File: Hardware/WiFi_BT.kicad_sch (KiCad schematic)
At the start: 12 parts, among them J5 Conn_01x12, P1 ESP_DATA, SW5 ESP_BOOT, SW6 ESP_RST, U7 ESP32-S3-WROOM-1

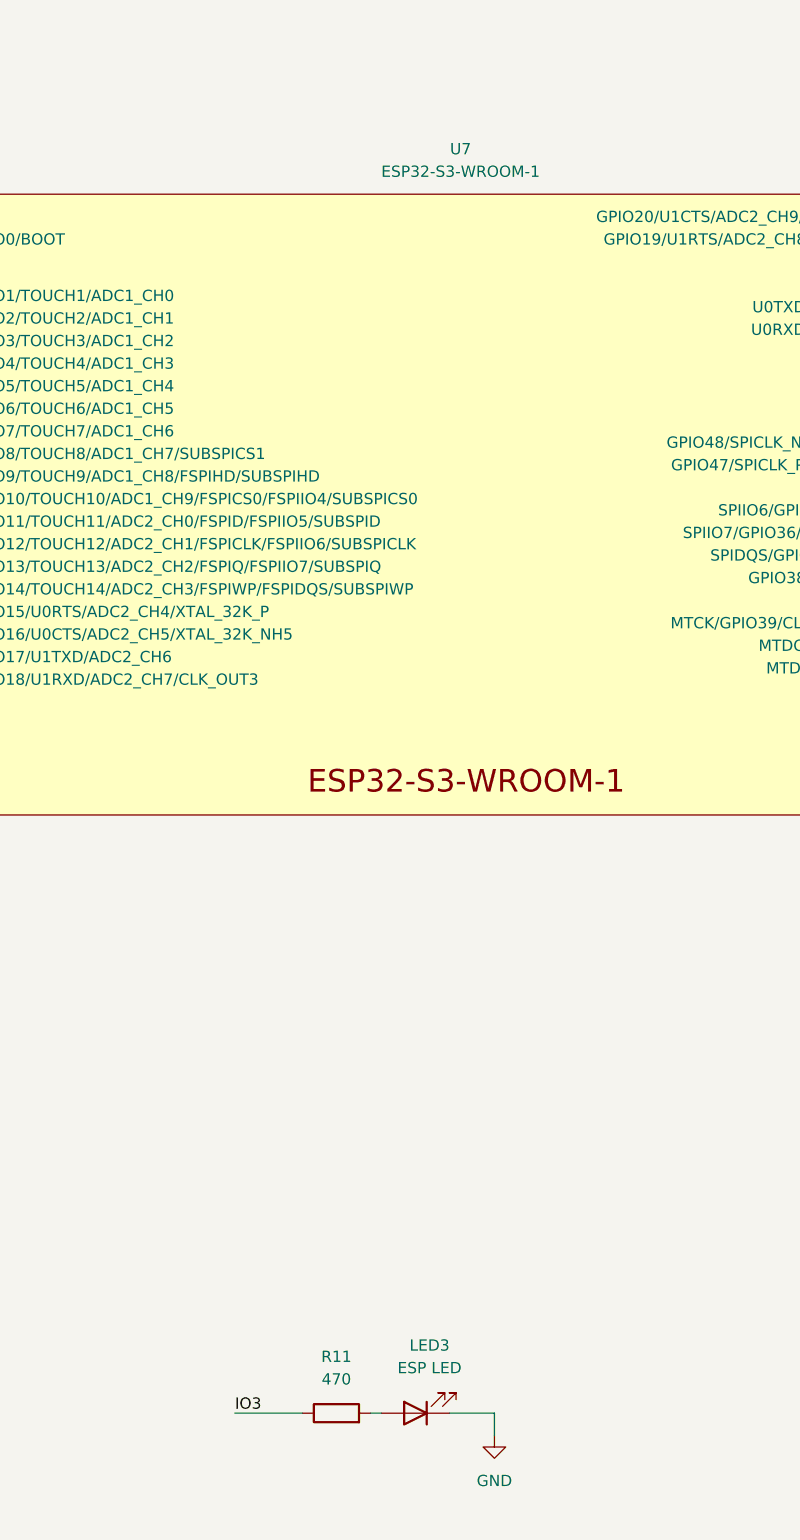
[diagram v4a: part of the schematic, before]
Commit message: TODO list completed - need to search for components
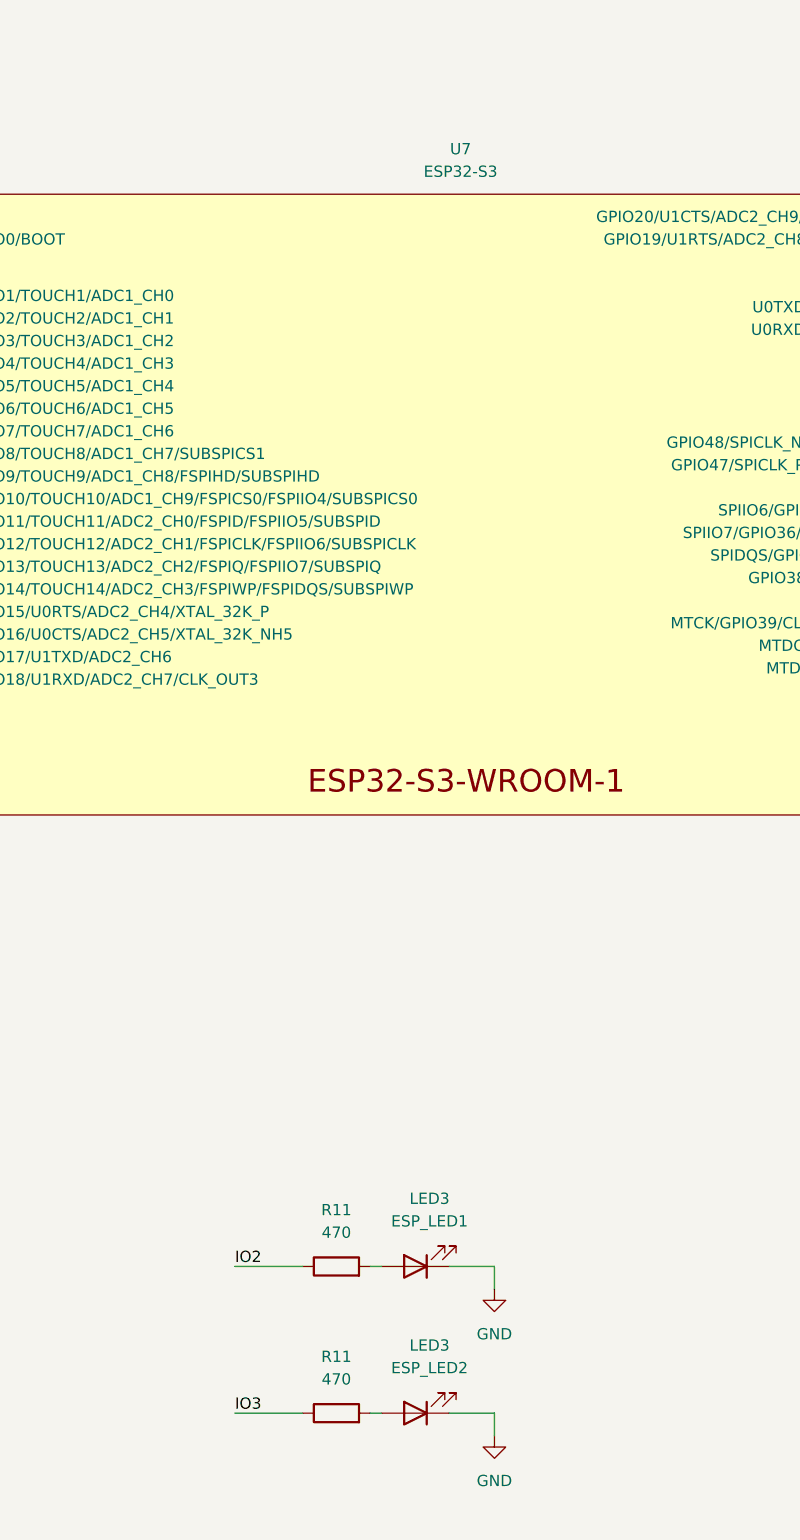
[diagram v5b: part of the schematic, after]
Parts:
- added LED3: ESP_LED1, LED_SMD:LED_0603_1608Metric, symbol Device:LED
- added R11: 470, Resistor_SMD:R_0402_1005Metric, symbol Device:R
- J5: footprint Connector_PinSocket_1.27mm:PinSocket_2x17_P1.27mm_Vertical -> Connector_PinSocket_1.27mm:PinSocket_2x16_P1.27mm_Vertical
- LED3: value ESP LED -> ESP_LED2
- U7: value ESP32-S3-WROOM-1 -> ESP32-S3
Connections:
- net GND: now also LED3.1 (K)
- net IO2: now also R11.1
- new net: LED3.2 (A), R11.2
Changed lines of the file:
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@@
   (junction (at 68.58 46.99) (diameter 0) (color 0 0 0 0)
   )
+  (wire (pts (xy 111.125 162.56) (xy 118.745 162.56))
+    (stroke (width 0) (type default))
+  )
   (wire (pts (xy 69.85 93.98) (xy 77.47 93.98))
     (stroke (width 0) (type default))
@@
     (stroke (width 0) (type default))
   )
+  (wire (pts (xy 140.335 162.56) (xy 140.335 165.1))
+    (stroke (width 0) (type default))
+  )
   (wire (pts (xy 195.58 54.61) (xy 208.28 54.61))
     (stroke (width 0) (type default))
@@
     (stroke (width 0) (type default))
   )
+  (wire (pts (xy 126.365 162.56) (xy 127.635 162.56))
+    (stroke (width 0) (type default))
+  )
   (wire (pts (xy 195.58 57.15) (xy 208.28 57.15))
     (stroke (width 0) (type default))
@@
   )
   (wire (pts (xy 195.58 92.71) (xy 203.2 92.71))
+    (stroke (width 0) (type default))
+  )
+  (wire (pts (xy 135.255 162.56) (xy 140.335 162.56))
     (stroke (width 0) (type default))
   )
@@
     (effects (font (size 1.27 1.27)) (justify right bottom))
   )
+  (label "IO2" (at 111.125 162.56 0) (fields_autoplaced)
+    (effects (font (size 1.27 1.27)) (justify left bottom))
+  )
   (label "IO40" (at 267.97 44.45 180) (fields_autoplaced)
     (effects (font (size 1.27 1.27)) (justify right bottom))
@@
       (effects (font (size 1.27 1.27)))
     )
-    (property "Value" "ESP LED" (at 133.0325 173.99 0)
+    (property "Value" "ESP_LED2" (at 133.0325 173.99 0)
       (effects (font (size 1.27 1.27)))
     )
@@
     )
   )
+  (symbol (lib_id "Device:R") (at 122.555 162.56 90) (unit 1)
+    (in_bom yes) (on_board yes) (dnp no) (fields_autoplaced)
+    (property "Reference" "R11" (at 122.555 156.21 90)
+      (effects (font (size 1.27 1.27)))
+    )
+    (property "Value" "470" (at 122.555 158.75 90)
+      (effects (font (size 1.27 1.27)))
+    )
+    (property "Footprint" "Resistor_SMD:R_0402_1005Metric" (at 122.555 164.338 90)
+      (effects (font (size 1.27 1.27)) hide)
+    )
+    (property "Datasheet" "~" (at 122.555 162.56 0)
+      (effects (font (size 1.27 1.27)) hide)
+    )
+    (pin "1")
+    (pin "2")
+    (instances
+      (project "Badge"
+        (path "/11e70834-763a-4962-b37c-877b60a06e6a"
+          (reference "R11") (unit 1)
+        )
+        (path "/11e70834-763a-4962-b37c-877b60a06e6a/439e12f3-d6d7-4417-89eb-793f278686d2"
+          (reference "R27") (unit 1)
+        )
+      )
+    )
+  )
   (symbol (lib_id "ESP32:ESP32-S3-WROOM-1") (at 137.16 76.2 0) (unit 1)
     (in_bom yes) (on_board yes) (dnp no) (fields_autoplaced)
@@
       (effects (font (size 1.27 1.27)))
     )
-    (property "Value" "ESP32-S3-WROOM-1" (at 136.525 39.37 0)
+    (property "Value" "ESP32-S3" (at 136.525 39.37 0)
       (effects (font (size 1.27 1.27)))
     )
@@
       (effects (font (size 1.27 1.27)))
     )
-    (property "Footprint" "Connector_PinSocket_1.27mm:PinSocket_2x17_P1.27mm_Vertical" (at 255.27 54.61 0)
+    (property "Footprint" "Connector_PinSocket_1.27mm:PinSocket_2x16_P1.27mm_Vertical" (at 255.27 54.61 0)
       (effects (font (size 1.27 1.27)) hide)
     )
@@
     )
   )
+  (symbol (lib_id "Device:LED") (at 131.445 162.56 180) (unit 1)
+    (in_bom yes) (on_board yes) (dnp no) (fields_autoplaced)
+    (property "Reference" "LED3" (at 133.0325 154.94 0)
+      (effects (font (size 1.27 1.27)))
+    )
+    (property "Value" "ESP_LED1" (at 133.0325 157.48 0)
+      (effects (font (size 1.27 1.27)))
+    )
+    (property "Footprint" "LED_SMD:LED_0603_1608Metric" (at 131.445 162.56 0)
+      (effects (font (size 1.27 1.27)) hide)
+    )
+    (property "Datasheet" "~" (at 131.445 162.56 0)
+      (effects (font (size 1.27 1.27)) hide)
+    )
+    (pin "1")
+    (pin "2")
+    (instances
+      (project "Badge"
+        (path "/11e70834-763a-4962-b37c-877b60a06e6a"
+          (reference "LED3") (unit 1)
+        )
+        (path "/11e70834-763a-4962-b37c-877b60a06e6a/439e12f3-d6d7-4417-89eb-793f278686d2"
+          (reference "LED4") (unit 1)
+        )
+      )
+    )
+  )
   (symbol (lib_id "Device:C") (at 55.88 57.15 180) (unit 1)
     (in_bom yes) (on_board yes) (dnp no)
@@
         )
       )
+    )
+  )
+  (symbol (lib_id "power:GND") (at 140.335 165.1 0) (unit 1)
+    (in_bom yes) (on_board yes) (dnp no) (fields_autoplaced)
+    (property "Reference" "#PWR026" (at 140.335 171.45 0)
+      (effects (font (size 1.27 1.27)) hide)
+    )
+    (property "Value" "GND" (at 140.335 170.18 0)
+      (effects (font (size 1.27 1.27)))
+    )
+    (property "Footprint" "" (at 140.335 165.1 0)
+      (effects (font (size 1.27 1.27)) hide)
+    )
+    (property "Datasheet" "" (at 140.335 165.1 0)
+      (effects (font (size 1.27 1.27)) hide)
+    )
+    (pin "1")
+    (instances
+      (project "Badge"
+        (path "/11e70834-763a-4962-b37c-877b60a06e6a"
+          (reference "#PWR026") (unit 1)
+        )
+        (path "/11e70834-763a-4962-b37c-877b60a06e6a/439e12f3-d6d7-4417-89eb-793f278686d2"
+          (reference "#PWR032") (unit 1)
+        )
+      )
